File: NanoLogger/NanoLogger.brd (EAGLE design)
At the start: 160 x 100 mm, 18 parts, among them IC1 TINY11S, U4 LIS331

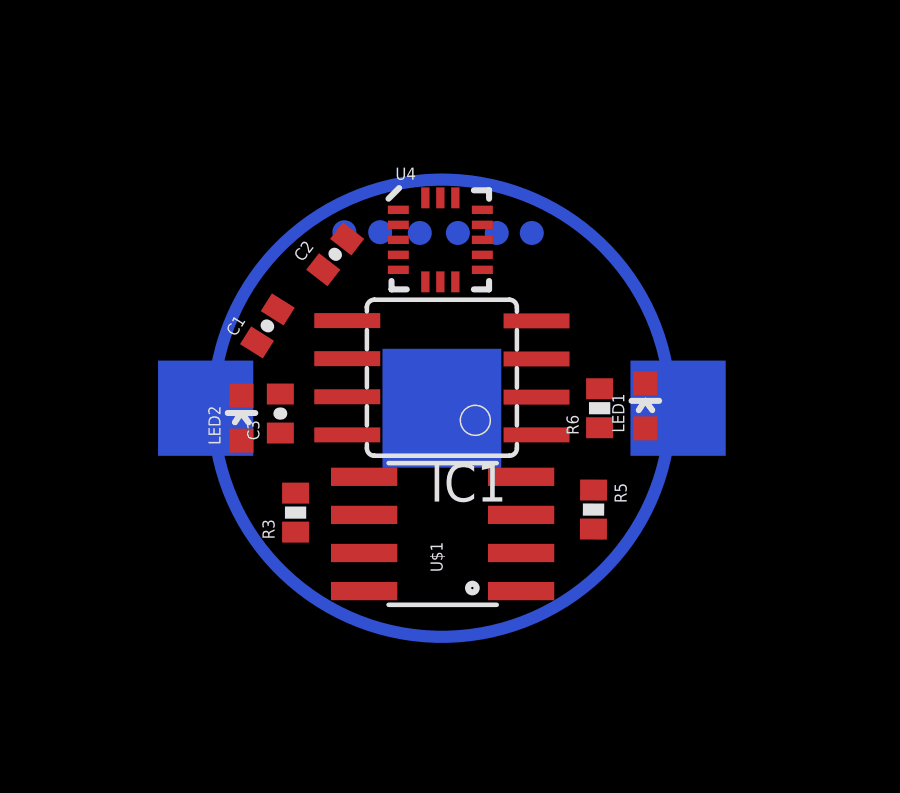
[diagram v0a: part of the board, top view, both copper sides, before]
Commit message: Updated and rerouted V1.1, early nanologger layout
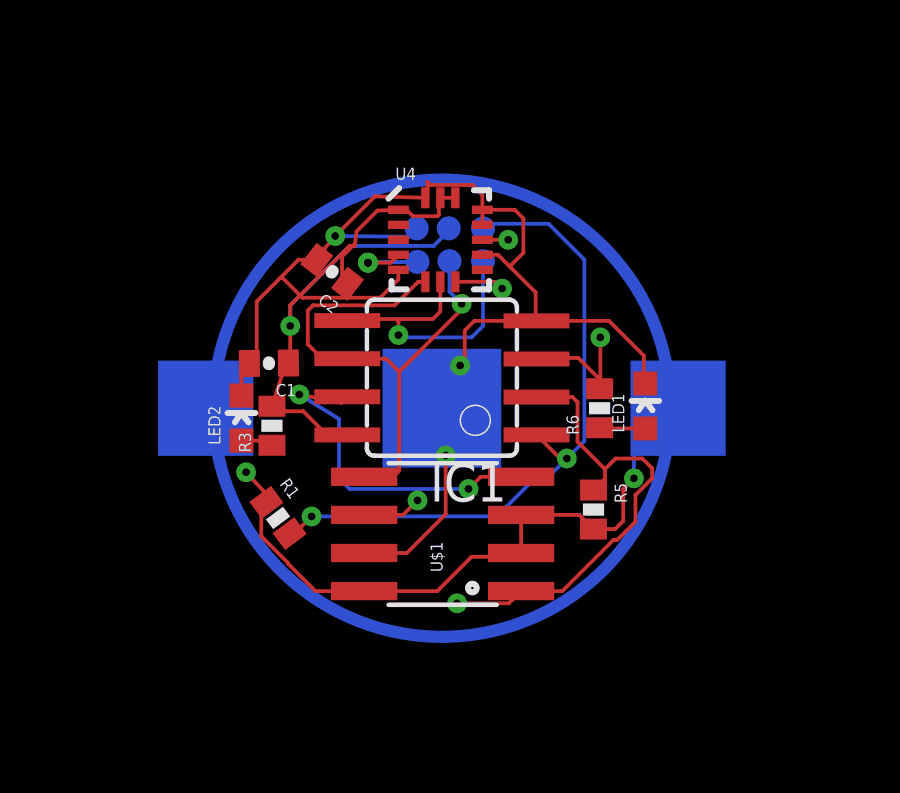
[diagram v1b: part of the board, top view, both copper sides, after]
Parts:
- removed C3: 10uF, SparkFun:0402-CAP
- added R1: 4.7k, SparkFun:0402-RES
- moved R3 3.00 mm to (10.8, 24.8)
- moved GND 2.42 mm to (15.7, 31.4)
- moved VCC 2.29 mm to (16.7, 31.4)
- moved CS 2.11 mm to (17.9, 31.4)
- moved MOSI 1.88 mm to (17.9, 30.3)
- moved MISO 1.83 mm to (16.8, 30.3)
- moved SCK 1.66 mm to (15.7, 30.3)
- moved C1 1.25 mm to (10.7, 26.9), turned to 180.6 degrees
- moved C2 0.59 mm to (12.9, 29.9), turned to 142.2 degrees
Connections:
- removed net N$4: IC1.2, R5.1, U$1.1
- new net N$2: CS.TP, IC1.1, R1.2
- net GND: no longer C3.2
- net N$11: now also IC1.2, R5.1, U$1.1; no longer IC1.3
- net N$12: now also IC1.3; no longer CS.TP, IC1.1
- net VCC: now also R1.1; no longer C3.1
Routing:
- net VCC: track 0.00 -> 50.1 mm, vias 0 -> 3
- net GND: track 0.00 -> 45.5 mm, vias 0 -> 3
- net N$11: track 0.00 -> 28.7 mm, vias 0 -> 2
- net N$2: track 0.00 -> 22.4 mm, vias 0 -> 2
- net N$5: track 0.00 -> 21.6 mm, vias 0 -> 4
- net N$7: track 0.00 -> 18.2 mm, vias 0 -> 1
- net N$6: track 0.00 -> 17.7 mm, vias 0 -> 2
- net N$12: track 0.00 -> 12.0 mm, vias 0 -> 2
- net N$10: track 0.00 -> 1.53 mm
- net N$3: track 0.00 -> 1.34 mm

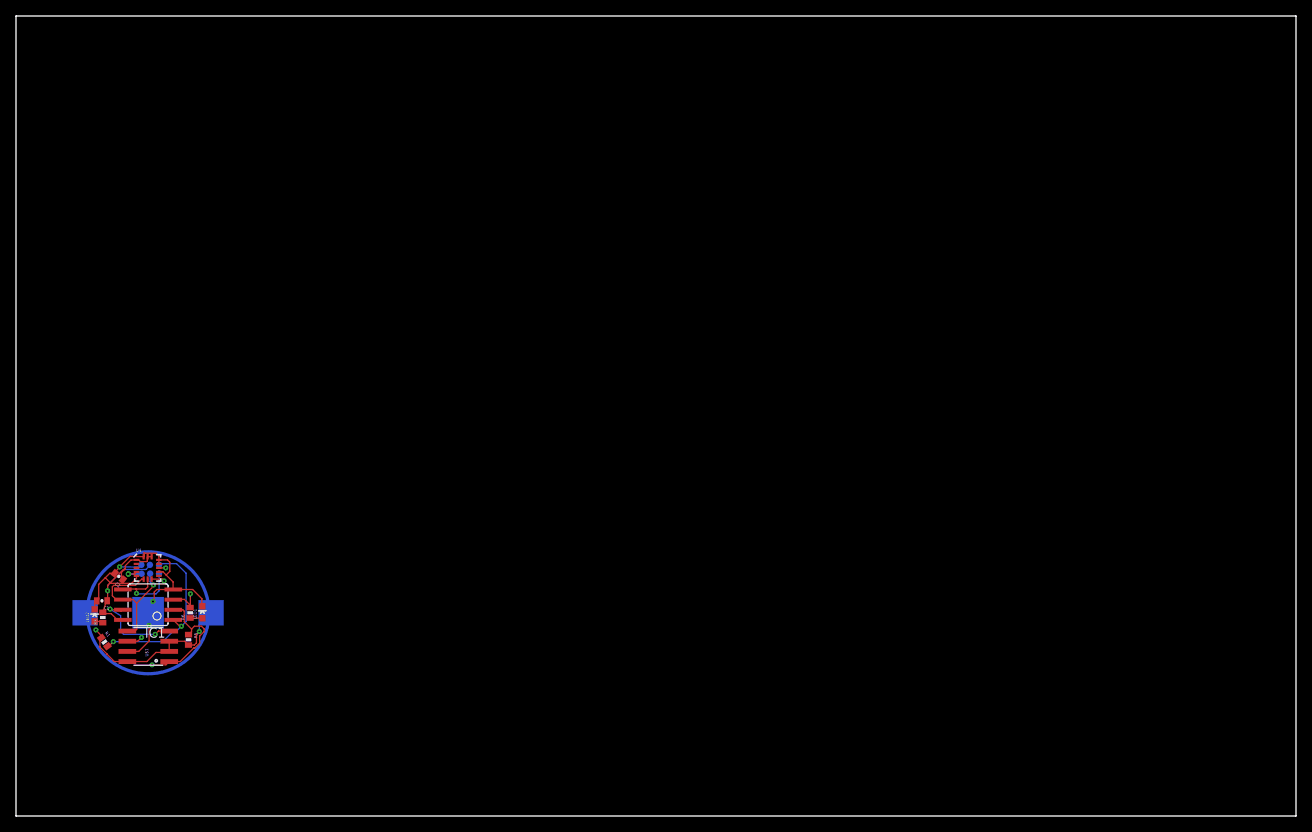
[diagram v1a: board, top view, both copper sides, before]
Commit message: NanoLogger is routed and ready for order. 16mm!
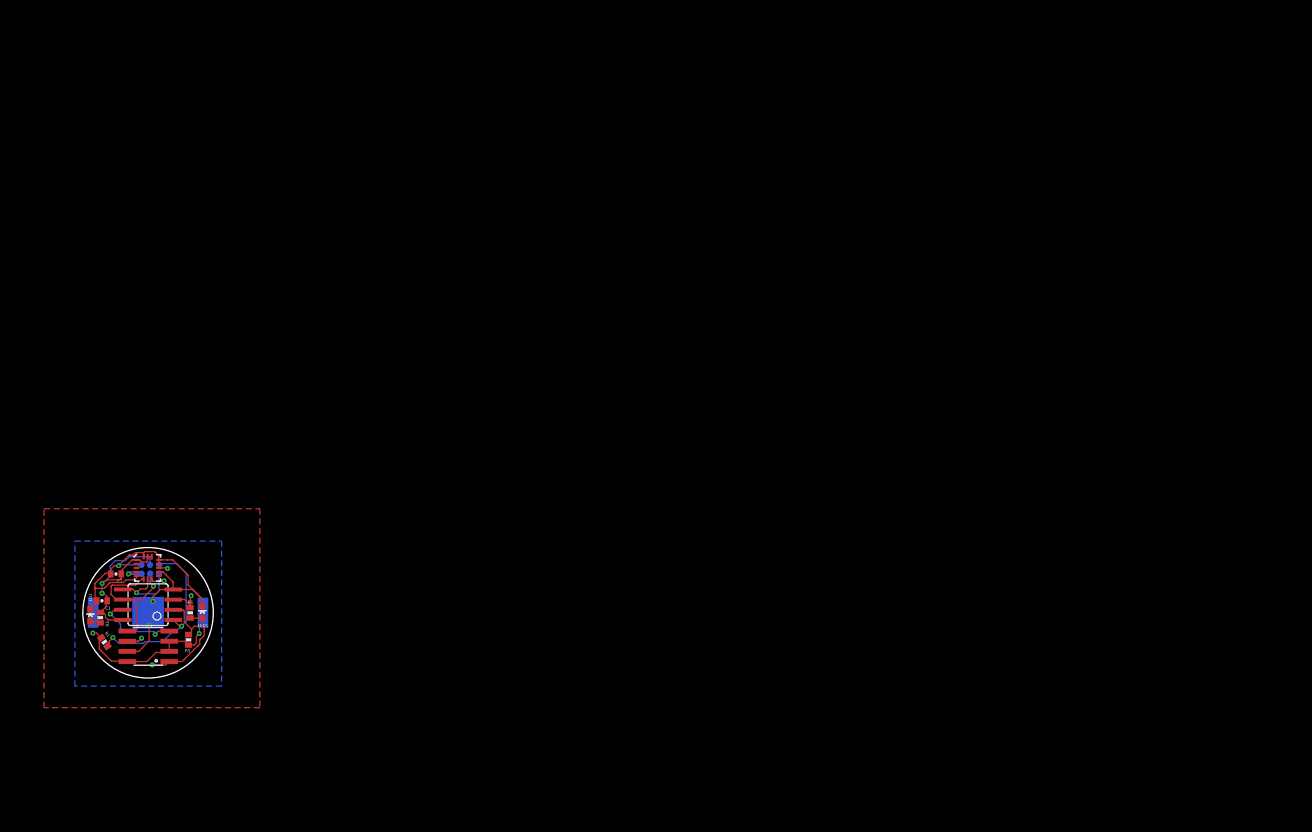
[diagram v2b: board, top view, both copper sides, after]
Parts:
- moved LED2 0.53 mm to (9.30, 25.1)
- moved C2 0.47 mm to (12.5, 30.3), turned to 181 degrees
- moved R3 0.31 mm to (10.5, 24.8)
- turned C1 to 180 degrees
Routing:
- net GND: track 45.5 -> 53.4 mm
- net VCC: track 50.1 -> 53.9 mm, vias 3 -> 4
- net N$2: track 22.4 -> 23.4 mm
- net N$7: track 18.2 -> 18.8 mm
- net N$5: track 21.6 -> 21.1 mm, vias 4 -> 3
- added copper zone on layer 16, net GND
- added copper zone on layer 1, net VCC
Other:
- board size 160 x 100 mm -> 16.3 x 16.3 mm

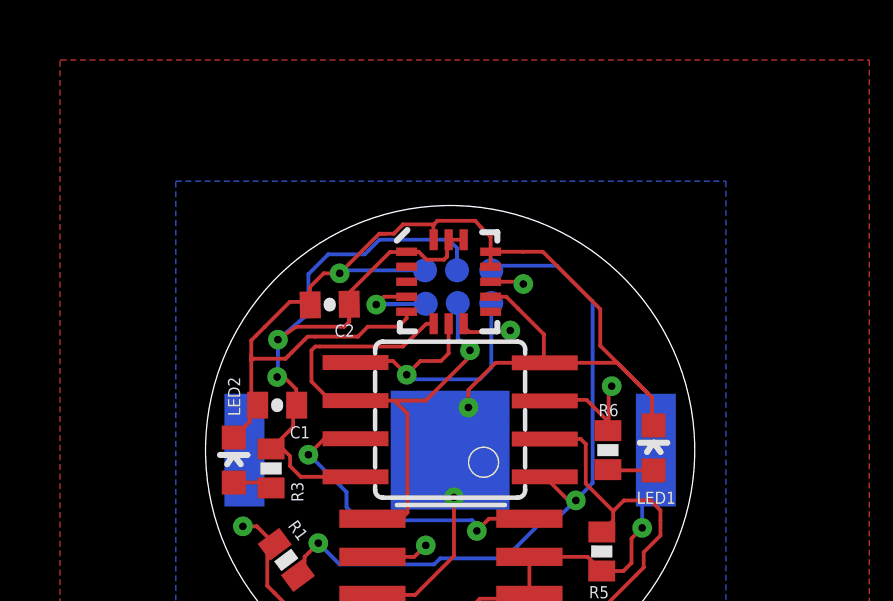
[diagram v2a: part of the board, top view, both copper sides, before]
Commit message: Updated readme, test code kinda works now
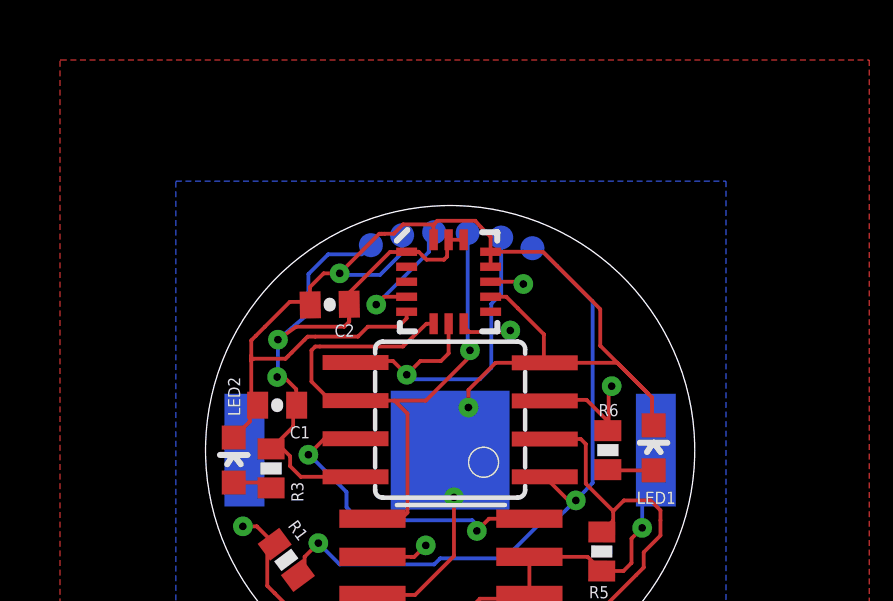
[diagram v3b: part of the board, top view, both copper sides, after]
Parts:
- moved VCC 2.99 mm to (13.9, 32.2)
- moved SCK 2.40 mm to (16.0, 32.7)
- moved MISO 2.36 mm to (17.1, 32.6)
- moved MOSI 2.21 mm to (18.2, 32.5)
- moved CS 1.56 mm to (19.3, 32.1)
- moved GND 1.39 mm to (14.9, 32.6)
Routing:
- net VCC: track 53.9 -> 50.8 mm
- net N$6: track 17.7 -> 20.0 mm
- net N$7: track 18.8 -> 21.0 mm
- net N$2: track 23.4 -> 22.2 mm
